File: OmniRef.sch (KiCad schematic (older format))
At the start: 45 parts, among them J1 4mm Banana Jack Pair, J2 4mm Banana Jack Pair, Q1 PMBT3906, SW1 SW_DPDT_x2, U1 REFERENCE IC, U2 LP2951, U3 REFERENCE IC, U4 AP3015

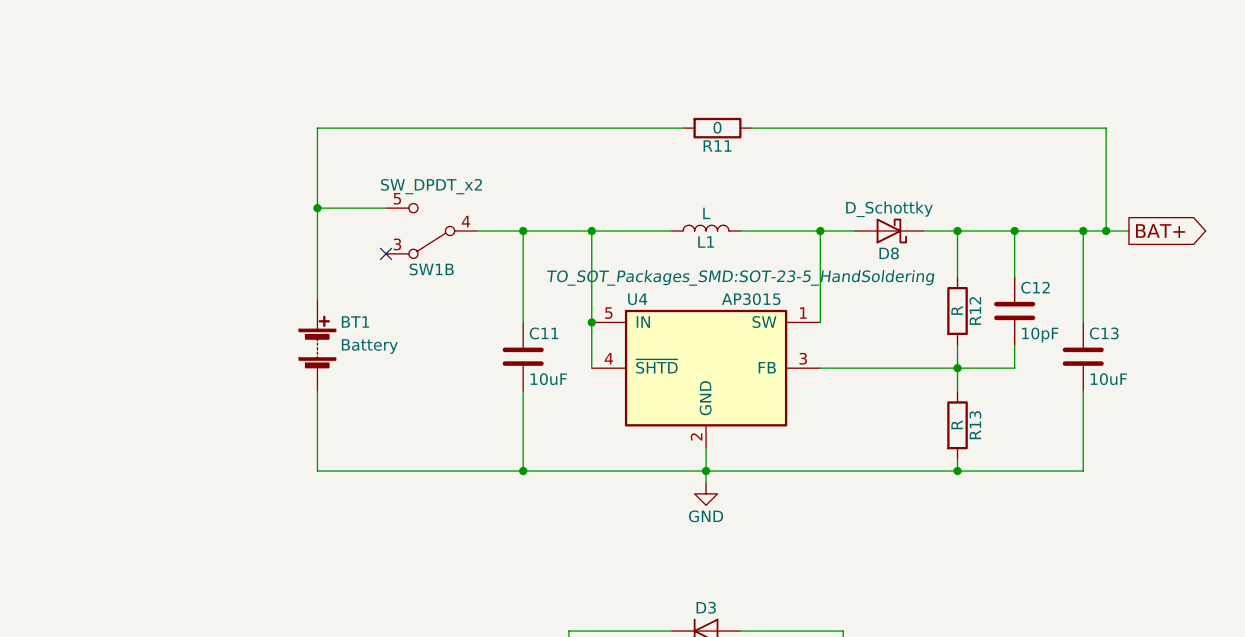
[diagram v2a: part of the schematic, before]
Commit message: Adjusted size of outline to improve board fit.
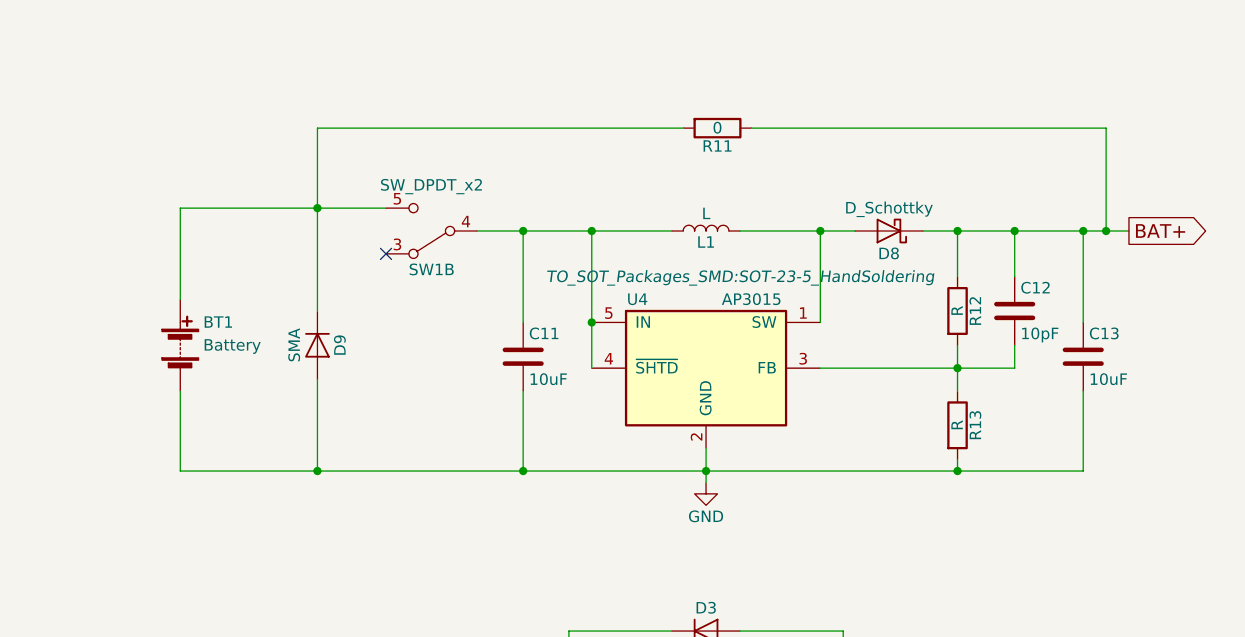
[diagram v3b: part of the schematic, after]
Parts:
- added D9: SMA, Diodes_SMD:D_SMA, symbol D
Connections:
- net GND: now also D9.2 (A)
- net at BT1.1 (+), R11.2, SW1.5 (C): now also D9.1 (K)
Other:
- moved on the sheet: BT1
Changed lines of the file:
@@
 L Battery BT1
 U 1 1 5A2175D4
-P 1500 1850
-F 0 "BT1" H 1600 1950 50  0000 L CNN
-F 1 "Battery" H 1600 1850 50  0000 L CNN
-F 2 "_NTSFootprints:9vClipWireLeads" V 1500 1910 50  0001 C CNN
-F 3 "" V 1500 1910 50  0000 C CNN
-	1    1500 1850
+P 900 1850
+F 0 "BT1" H 1000 1950 50  0000 L CNN
+F 1 "Battery" H 1000 1850 50  0000 L CNN
+F 2 "_NTSFootprints:9vClipWireLeads" V 900 1910 50  0001 C CNN
+F 3 "" V 900 1910 50  0000 C CNN
+	1    900  1850
 	1    0    0    -1
 $EndComp
@@
 $EndComp
 Wire Wire Line
-	1500 2400 4850 2400
+	900  2400 4850 2400
 Connection ~ 3200 2400
 Connection ~ 2400 1350
@@
 Connection ~ 2400 2400
 Wire Wire Line
-	1500 1250 1800 1250
-Wire Wire Line
-	1500 900  1500 1650
-Wire Wire Line
-	1500 2050 1500 2400
+	900  1250 1800 1250
+Wire Wire Line
+	1500 900  1500 1700
+Wire Wire Line
+	1500 2000 1500 2400
 Wire Wire Line
 	2400 1750 2400 1350
@@
 	4950 900  4950 1350
 Connection ~ 4950 1350
+$Comp
+L D D9
+U 1 1 5A3B30FB
+P 1500 1850
+F 0 "D9" H 1500 1950 50  0000 C CNN
+F 1 "SMA" H 1500 1750 50  0000 C CNN
+F 2 "Diodes_SMD:D_SMA" H 1500 1850 50  0001 C CNN
+F 3 "" H 1500 1850 50  0000 C CNN
+	1    1500 1850
+	0    1    1    0
+$EndComp
+Wire Wire Line
+	900  2050 900  2400
+Connection ~ 1500 2400
+Wire Wire Line
+	900  1650 900  1250
 $EndSCHEMATC

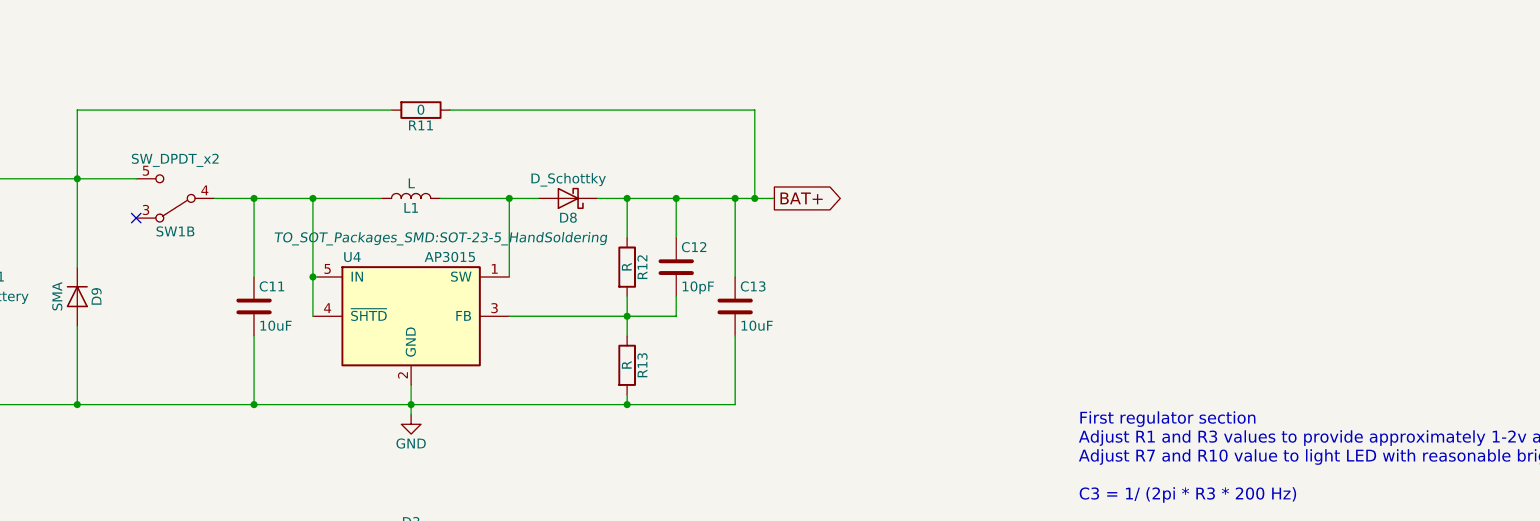
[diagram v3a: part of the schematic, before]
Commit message: Selected resistors for switching regulator.  Fixed SW1 wiring.
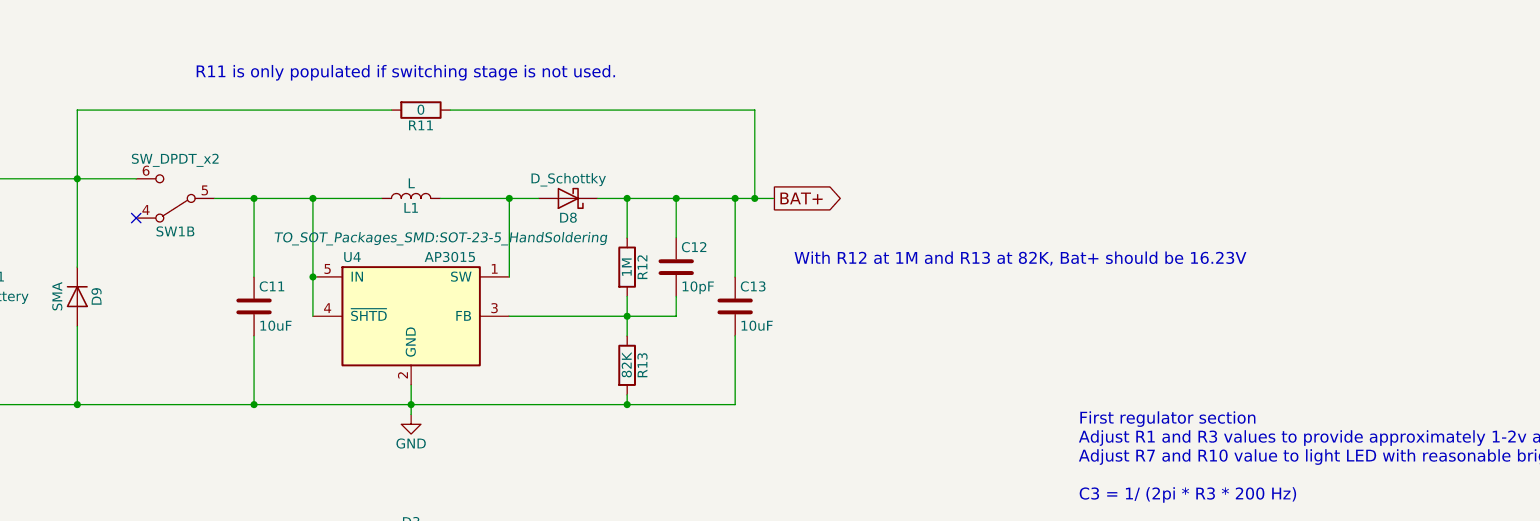
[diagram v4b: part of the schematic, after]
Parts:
- removed SW1: SW_DPDT_x2, _NTSFootprints:CnK_L_Series_DPDT, symbol SW_DPDT_x2
- added SW1: SW_DPDT_x2, _NTSFootprints:CnK_L_Series_DPDT, symbol SW_DPDT_x2_CORRECT
- R12: value R -> 1M
- R13: value R -> 82K
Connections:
- net BAT+: now also SW1.3 (C)
- net at D1.1 (K): now also SW1.1 (A)
- net at C2.1, D3.1 (K), D4.1 (K)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: now also SW1.2 (B)
- net at BT1.1 (+), D9.1 (K), R11.2: now also SW1.6 (C)
- net at C11.1, L1.1, U4.4 (~SHTD)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: now also SW1.5 (B)
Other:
- note added: "R11 is only populated if switching stage is not used."
- note added: "With R12 at 1M and R13 at 82K, Bat+ should be 16.23V"
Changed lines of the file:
@@
-$EndComp
-$Comp
-L SW_DPDT_x2 SW1
-U 1 1 5A37F64C
-P 2000 3450
-F 0 "SW1" H 2000 3620 50  0000 C CNN
-F 1 "SW_DPDT_x2" H 2000 3250 50  0000 C CNN
-F 2 "_NTSFootprints:CnK_L_Series_DPDT" H 2000 3450 50  0001 C CNN
-F 3 "" H 2000 3450 50  0000 C CNN
-	1    2000 3450
-	-1   0    0    1
-$EndComp
-$Comp
-L SW_DPDT_x2 SW1
-U 2 1 5A37F91F
-P 2000 1350
-F 0 "SW1" H 2000 1520 50  0000 C CNN
-F 1 "SW_DPDT_x2" H 2000 1150 50  0000 C CNN
-F 2 "_NTSFootprints:CnK_L_Series_DPDT" H 2000 1350 50  0001 C CNN
-F 3 "" H 2000 1350 50  0000 C CNN
-	2    2000 1350
-	-1   0    0    1
 $EndComp
 $Comp
@@
 P 4300 1700
 F 0 "R12" V 4380 1700 50  0000 C CNN
-F 1 "R" V 4300 1700 50  0000 C CNN
+F 1 "1M" V 4300 1700 50  0000 C CNN
 F 2 "Resistors_SMD:R_0805_HandSoldering" V 4230 1700 50  0001 C CNN
 F 3 "" H 4300 1700 50  0000 C CNN
@@
 P 4300 2200
 F 0 "R13" V 4380 2200 50  0000 C CNN
-F 1 "R" V 4300 2200 50  0000 C CNN
+F 1 "82K" V 4300 2200 50  0000 C CNN
 F 2 "Resistors_SMD:R_0805_HandSoldering" V 4230 2200 50  0001 C CNN
 F 3 "" H 4300 2200 50  0000 C CNN
@@
 Wire Wire Line
 	900  1650 900  1250
+Text Notes 5150 1700 0    60   ~ 0
+With R12 at 1M and R13 at 82K, Bat+ should be 16.23V
+Text Notes 2100 750  0    60   ~ 0
+R11 is only populated if switching stage is not used.
+$Comp
+L SW_DPDT_x2_CORRECT SW1
+U 1 1 5A40F794
+P 2000 3450
+F 0 "SW1" H 2000 3620 50  0000 C CNN
+F 1 "SW_DPDT_x2" H 2000 3250 50  0000 C CNN
+F 2 "_NTSFootprints:CnK_L_Series_DPDT" H 2000 3450 50  0001 C CNN
+F 3 "" H 2000 3450 50  0000 C CNN
+	1    2000 3450
+	-1   0    0    1
+$EndComp
+$Comp
+L SW_DPDT_x2_CORRECT SW1
+U 2 1 5A40FADF
+P 2000 1350
+F 0 "SW1" H 2000 1520 50  0000 C CNN
+F 1 "SW_DPDT_x2" H 2000 1150 50  0000 C CNN
+F 2 "_NTSFootprints:CnK_L_Series_DPDT" H 2000 1350 50  0001 C CNN
+F 3 "" H 2000 1350 50  0000 C CNN
+	2    2000 1350
+	-1   0    0    1
+$EndComp
 $EndSCHEMATC

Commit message: Fixed a number of issues discovered during prototyping.  Re-arranged logos a bit.
Moved RV1 between output jacks to clear battery.
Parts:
- removed D4: SMA, Diodes_SMD:D_SMA, symbol D
- R1: value 2.4K -> 10K
- R10, R7: value 1K -> 3.6K
- R3: value 270 -> 100K
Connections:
- net V+: now also Q1.2 (E); no longer Q1.3 (C)
- net at D5.2 (A): now also Q1.3 (C); no longer Q1.2 (E)
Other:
- note added: "Adjust R1 and R3 values to provide approximately 2v above reference output voltage.\nWith R3 at 100K and R1 at 10K, the voltage should be about 13.58V\nAdjust R7 and R10 value to light LED with reasonable brightness for the voltage chosen.\n3mA seems to be about right for the LED brightness."
- note added: "D6 is intended to clamp the output voltage if driven from an external source.\nIt also provides reverse voltage protection.\n\nR8 is to provide a fixed load for the regulator to work against and is probably not needed.\n\nOnly one output bypass cap is really needed. The different ones shown just\nprovide options if a particular reference needs a certain capacitance or ESR."
- note added: "R9 is only used for certain Linear Technology IC's that have a shutdown terminal.\n\nC10 is only used for certain Maxim Integrated IC's.\n\nC4 and C5 are optional stability improving capacitors.\nCheck the datasheet of the reference to see if one should be used.\n\nR2 and RV1 are to trim the output voltage on certain references."
- note removed: "D6 is intended to clamp the output voltage driven from an external source.\nIt also provides reverse voltage protection.\n\nR9 is to provide a fixed load for the regulator to work against.\n\nR6 and C7 act as a low frequency filter.\n\nD2 is to protect the IC if the output is driven from an external source."
- note removed: "First regulator section \nAdjust R1 and R3 values to provide approximately 1-2v above reference output voltage.\nAdjust R7 and R10 value to light LED with reasonable brightness for the voltage chosen.\n\nC3 = 1/ (2pi * R3 * 200 Hz)"
- note removed: "R9 is only used for certain linear technology ic's that have a shutdown terminal."
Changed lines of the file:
@@
 P 4150 4250
 F 0 "R1" V 4230 4250 50  0000 C CNN
-F 1 "2.4K" V 4150 4250 50  0000 C CNN
+F 1 "10K" V 4150 4250 50  0000 C CNN
 F 2 "Resistors_SMD:R_0805_HandSoldering" V 4080 4250 50  0001 C CNN
 F 3 "" H 4150 4250 50  0000 C CNN
@@
 P 4150 3850
 F 0 "R3" V 4230 3850 50  0000 C CNN
-F 1 "270" V 4150 3850 50  0000 C CNN
+F 1 "100K" V 4150 3850 50  0000 C CNN
 F 2 "Resistors_SMD:R_0805_HandSoldering" V 4080 3850 50  0001 C CNN
 F 3 "" H 4150 3850 50  0000 C CNN
@@
 	1    0    0    -1
 $EndComp
-Text Notes 6600 2900 0    60   ~ 0
-First regulator section \nAdjust R1 and R3 values to provide approximately 1-2v above reference output voltage.\nAdjust R7 and R10 value to light LED with reasonable brightness for the voltage chosen.\n\nC3 = 1/ (2pi * R3 * 200 Hz)
+Text Notes 4300 3250 0    60   ~ 0
+Adjust R1 and R3 values to provide approximately 2v above reference output voltage.\nWith R3 at 100K and R1 at 10K, the voltage should be about 13.58V\nAdjust R7 and R10 value to light LED with reasonable brightness for the voltage chosen.\n3mA seems to be about right for the LED brightness.
 $Comp
 L C C5
@@
 P 6550 4600
 F 0 "R7" V 6630 4600 50  0000 C CNN
-F 1 "1K" V 6550 4600 50  0000 C CNN
+F 1 "3.6K" V 6550 4600 50  0000 C CNN
 F 2 "Resistors_SMD:R_0805_HandSoldering" V 6480 4600 50  0001 C CNN
 F 3 "" H 6550 4600 50  0000 C CNN
@@
 	1    0    0    -1
 $EndComp
-Text Notes 1350 5100 0    60   ~ 0
-R9 is only used for certain linear technology ic's that have a shutdown terminal.
-Text Notes 7100 4050 0    60   ~ 0
-D6 is intended to clamp the output voltage driven from an external source.\nIt also provides reverse voltage protection.\n\nR9 is to provide a fixed load for the regulator to work against.\n\nR6 and C7 act as a low frequency filter.\n\nD2 is to protect the IC if the output is driven from an external source.
+Text Notes 6900 5450 0    60   ~ 0
+R9 is only used for certain Linear Technology IC's that have a shutdown terminal.\n\nC10 is only used for certain Maxim Integrated IC's.\n\nC4 and C5 are optional stability improving capacitors.\nCheck the datasheet of the reference to see if one should be used.\n\nR2 and RV1 are to trim the output voltage on certain references.
+Text Notes 6700 6300 0    60   ~ 0
+D6 is intended to clamp the output voltage if driven from an external source.\nIt also provides reverse voltage protection.\n\nR8 is to provide a fixed load for the regulator to work against and is probably not needed.\n\nOnly one output bypass cap is really needed.  The different ones shown just\nprovide options if a particular reference needs a certain capacitance or ESR.
 Wire Wire Line
 	-700 650  -700 750
@@
 F 3 "" H 6450 3850 50  0000 C CNN
 	1    6450 3850
-	1    0    0    -1
-$EndComp
-$Comp
-L D D4
-U 1 1 5A211331
-P 2200 4050
-F 0 "D4" H 2200 4150 50  0000 C CNN
-F 1 "SMA" H 2200 3950 50  0000 C CNN
-F 2 "Diodes_SMD:D_SMA" H 2200 4050 50  0001 C CNN
-F 3 "" H 2200 4050 50  0000 C CNN
-	1    2200 4050
-	0    1    1    0
-$EndComp
-Wire Wire Line
-	2200 4200 2200 4550
-Connection ~ 2200 4550
+	1    0    0    1
+$EndComp
 Wire Wire Line
 	2450 4200 2450 4550
@@
 Text GLabel 1350 3350 0    60   Input ~ 0
 BAT+
-Wire Wire Line
-	2200 3450 2200 3900
-Connection ~ 2200 3550
 Wire Wire Line
 	1800 3350 1350 3350
@@
 P 5250 4200
 F 0 "R10" V 5330 4200 50  0000 C CNN
-F 1 "1K" V 5250 4200 50  0000 C CNN
+F 1 "3.6K" V 5250 4200 50  0000 C CNN
 F 2 "Resistors_SMD:R_0805_HandSoldering" V 5180 4200 50  0001 C CNN
 F 3 "" H 5250 4200 50  0000 C CNN
@@
 	-1   0    0    1
 $EndComp
+Wire Wire Line
+	2200 3450 2200 3550
 $EndSCHEMATC

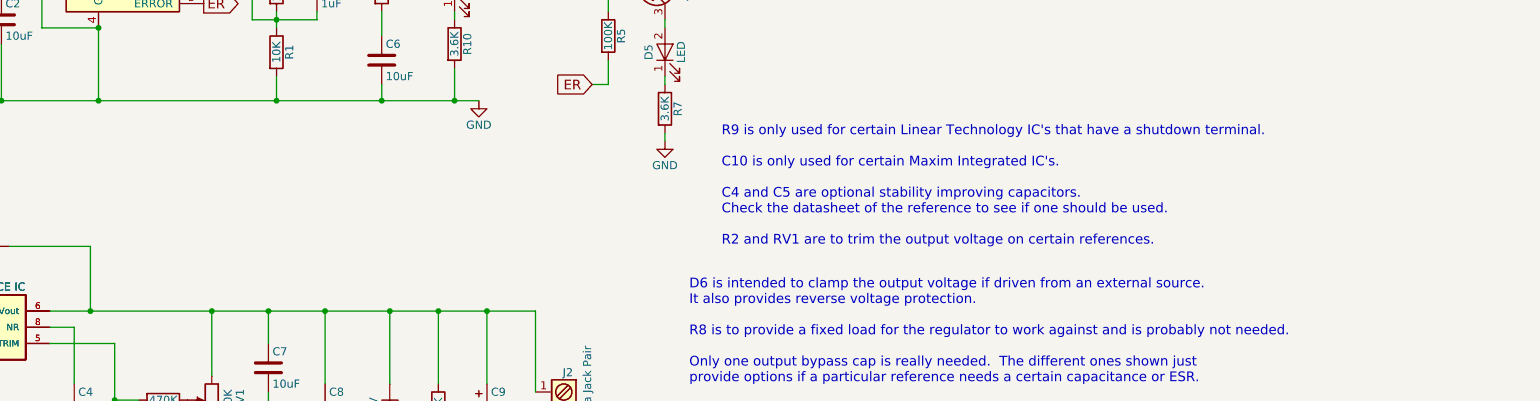
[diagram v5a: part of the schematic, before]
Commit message: Adjusted OSHW logo.
Made PDF's of the schematic and board.
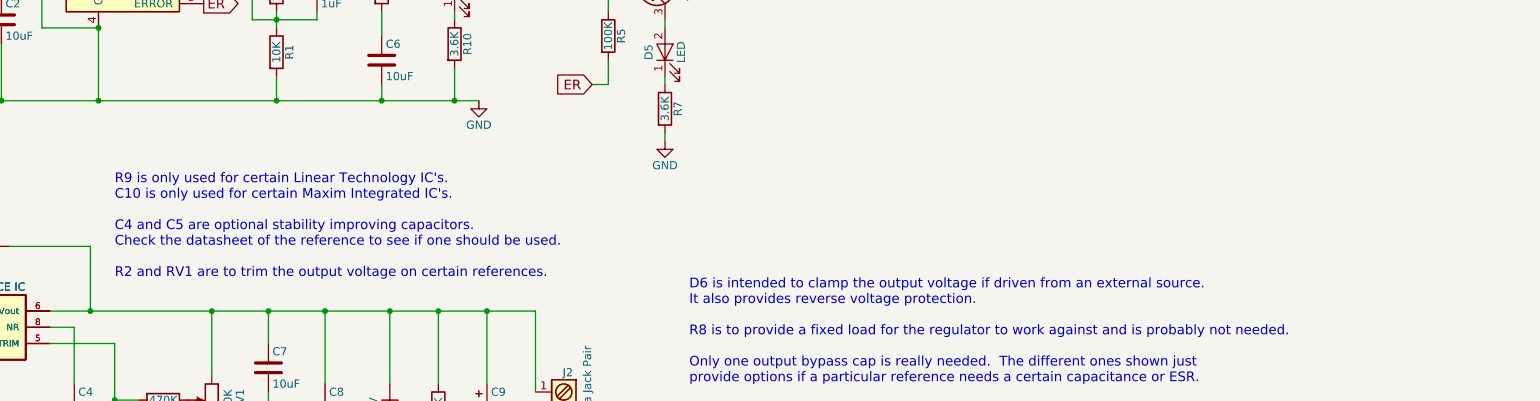
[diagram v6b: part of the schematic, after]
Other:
- note added: "R9 is only used for certain Linear Technology IC's.\nC10 is only used for certain Maxim Integrated IC's.\n\nC4 and C5 are optional stability improving capacitors.\nCheck the datasheet of the reference to see if one should be used.\n\nR2 and RV1 are to trim the output voltage on certain references."
- note removed: "R9 is only used for certain Linear Technology IC's that have a shutdown terminal.\n\nC10 is only used for certain Maxim Integrated IC's.\n\nC4 and C5 are optional stability improving capacitors.\nCheck the datasheet of the reference to see if one should be used.\n\nR2 and RV1 are to trim the output voltage on certain references."
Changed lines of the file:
@@
 encoding utf-8
 Sheet 1 1
-Title ""
-Date ""
-Rev ""
-Comp ""
-Comment1 ""
+Title "OmniRef"
+Date "2017-12-26"
+Rev "1"
+Comp "Schenktronics"
+Comment1 "Nathan Schenk"
 Comment2 ""
 Comment3 ""
@@
 	1    0    0    -1
 $EndComp
-Text Notes 6900 5450 0    60   ~ 0
-R9 is only used for certain Linear Technology IC's that have a shutdown terminal.\n\nC10 is only used for certain Maxim Integrated IC's.\n\nC4 and C5 are optional stability improving capacitors.\nCheck the datasheet of the reference to see if one should be used.\n\nR2 and RV1 are to trim the output voltage on certain references.
+Text Notes 3150 5650 0    60   ~ 0
+R9 is only used for certain Linear Technology IC's.\nC10 is only used for certain Maxim Integrated IC's.\n\nC4 and C5 are optional stability improving capacitors.\nCheck the datasheet of the reference to see if one should be used.\n\nR2 and RV1 are to trim the output voltage on certain references.
 Text Notes 6700 6300 0    60   ~ 0
 D6 is intended to clamp the output voltage if driven from an external source.\nIt also provides reverse voltage protection.\n\nR8 is to provide a fixed load for the regulator to work against and is probably not needed.\n\nOnly one output bypass cap is really needed.  The different ones shown just\nprovide options if a particular reference needs a certain capacitance or ESR.
